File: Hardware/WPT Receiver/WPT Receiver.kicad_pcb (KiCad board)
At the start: 2 copper layers, 100 x 100 mm, 151 parts, among them J1 0.1" Header, J2 Tag-connect-NL, J3 0.1" Header, J4 0.1" Header, SW1 PTS647, SW2 PTS647, SW3 PTS647, U1 STM32G031C6U6, U10 74HC595, U2 INA180A3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

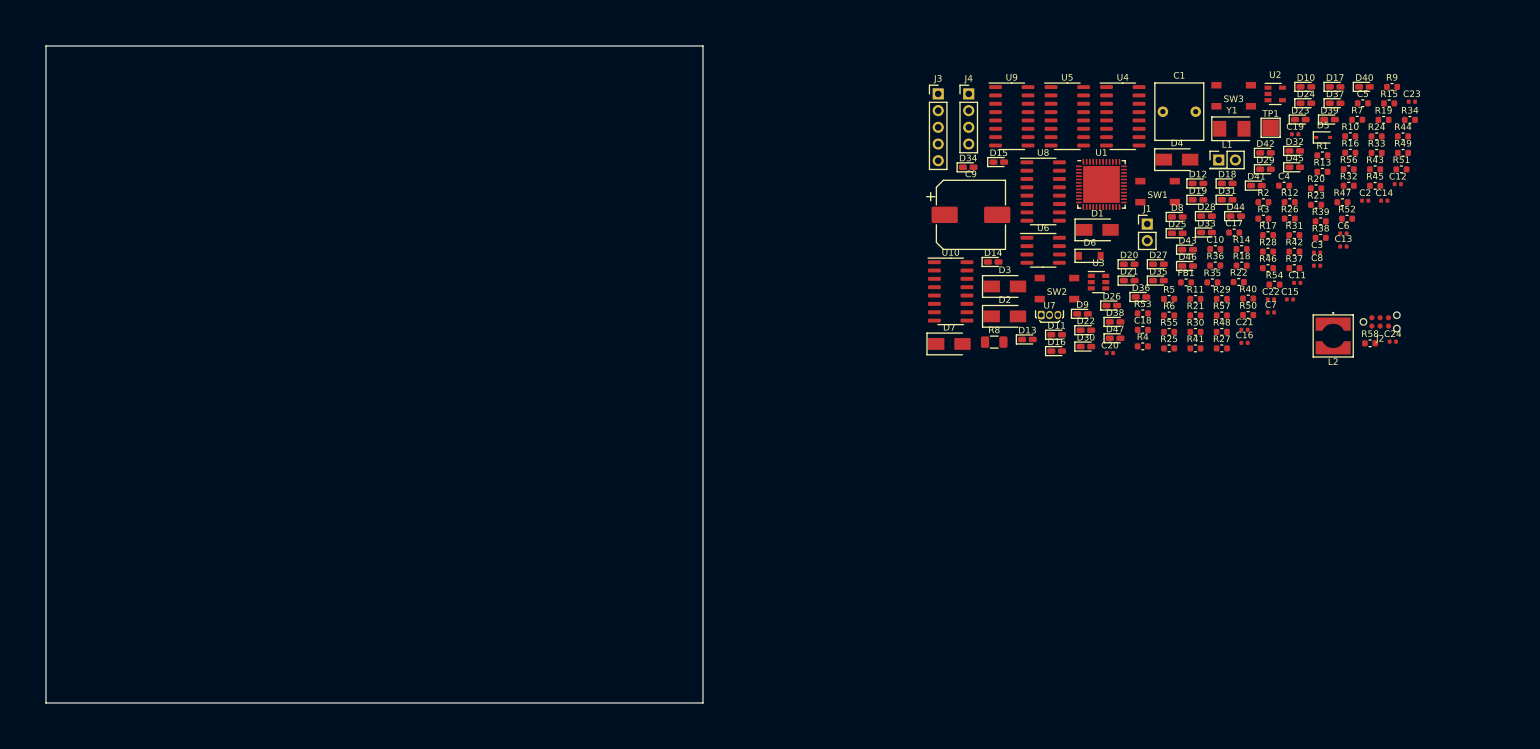
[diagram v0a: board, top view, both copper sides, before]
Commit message: started very rough part placement. Rounded board outline edges.
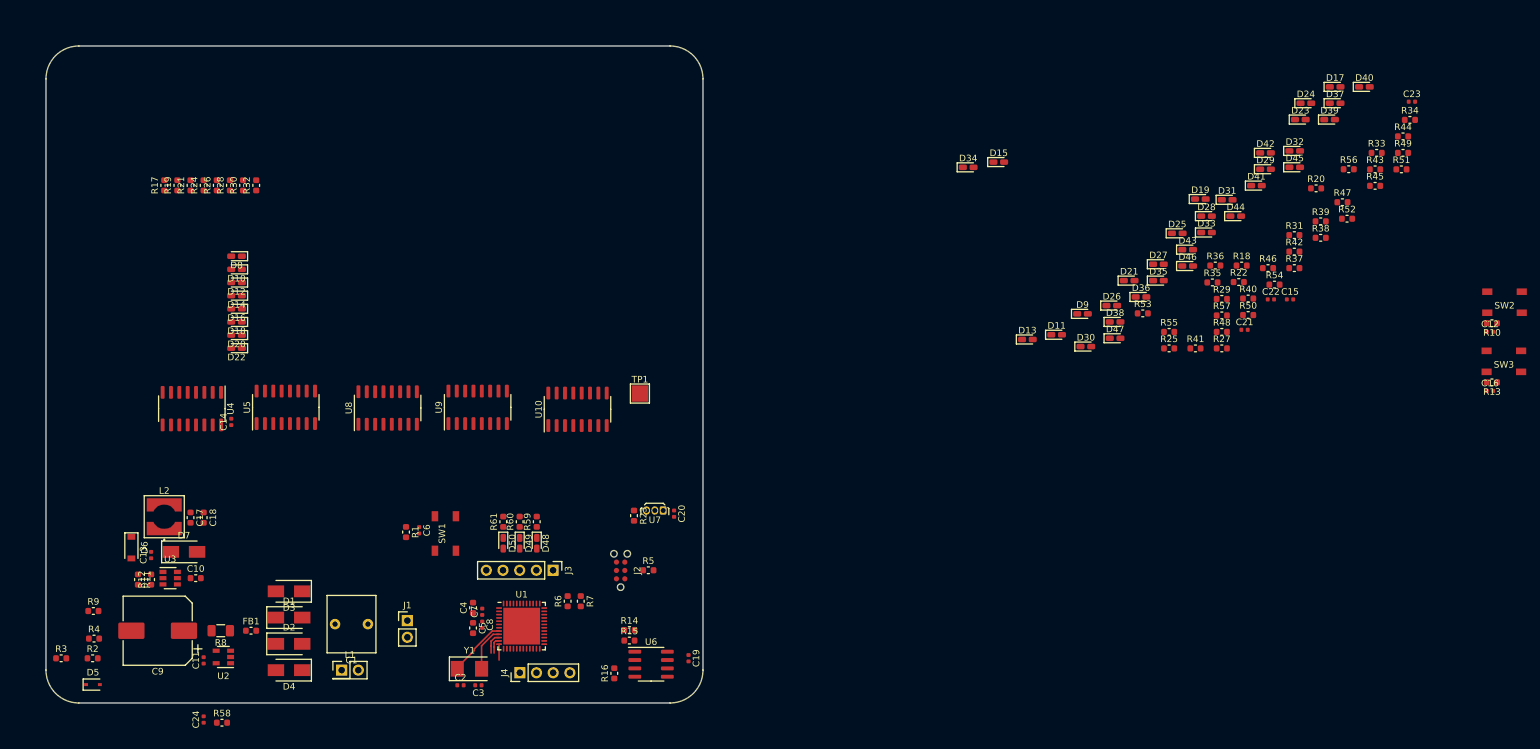
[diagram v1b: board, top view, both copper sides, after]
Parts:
- added D48: GRN, LED_SMD:LED_0603_1608Metric_Castellated, F.Cu at (124.7, 125.7)
- added D49: GRN, LED_SMD:LED_0603_1608Metric_Castellated, F.Cu at (122.1, 125.7)
- added D50: GRN, LED_SMD:LED_0603_1608Metric_Castellated, F.Cu at (119.6, 125.7)
- added R59: 680, Resistor_SMD:R_0603_1608Metric, F.Cu at (124.7, 122.4)
- added R60: 680, Resistor_SMD:R_0603_1608Metric, F.Cu at (122.1, 122.4)
- added R61: 680, Resistor_SMD:R_0603_1608Metric, F.Cu at (119.6, 122.4)
- moved R9 213.2 mm to (57.2, 136.0)
- moved D5 204.9 mm to (57.1, 147.2)
- moved R3 194.8 mm to (52.3, 143.2)
- moved R2 191.2 mm to (57.1, 143.2)
- moved C24 189.9 mm to (74.0, 152.5), turned to 90 degrees
- moved C13 187.5 mm to (66.0, 127.5), turned to 90 degrees
- moved R58 184.0 mm to (76.8, 153.0)
- moved R19 183.9 mm to (70.0, 71.2), turned to 90 degrees
- moved R12 182.6 mm to (66.0, 131.2), turned to 90 degrees
- moved U2 181.6 mm to (77.0, 143.0), turned to 180 degrees
- moved L2 180.0 mm to (68.0, 121.7), turned to 180 degrees
- moved C14 178.7 mm to (78.2, 107.2), turned to 90 degrees
- moved R24 178.7 mm to (74.0, 71.2), turned to 90 degrees
- moved C11 176.1 mm to (74.0, 143.5), turned to 90 degrees
- moved R17 168.2 mm to (68.0, 71.2), turned to 90 degrees
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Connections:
- net /GPIO1 renamed /LD1
- net /GPIO2 renamed /LD2
- net /GPIO3 renamed /LD3
- net Net-(D1-Pad1) renamed /VSYS_H
- net Net-(FB1-Pad1) renamed /VSYS_L
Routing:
- net Net-(C2-Pad1): track 0.00 -> 9.44 mm
- net Net-(C3-Pad1): track 0.00 -> 6.89 mm
- net /RST: track 0.00 -> 3.23 mm
- net /USER_BTN1: track 0.00 -> 2.47 mm
- net /ISENSE: track 0.00 -> 2.41 mm
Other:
- outline, holes or cut-outs redrawn

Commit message: Positioned non-power components, and routed most signals for peripherals other than shift regs/drivers. Added folder for 3D models for switch and crystal
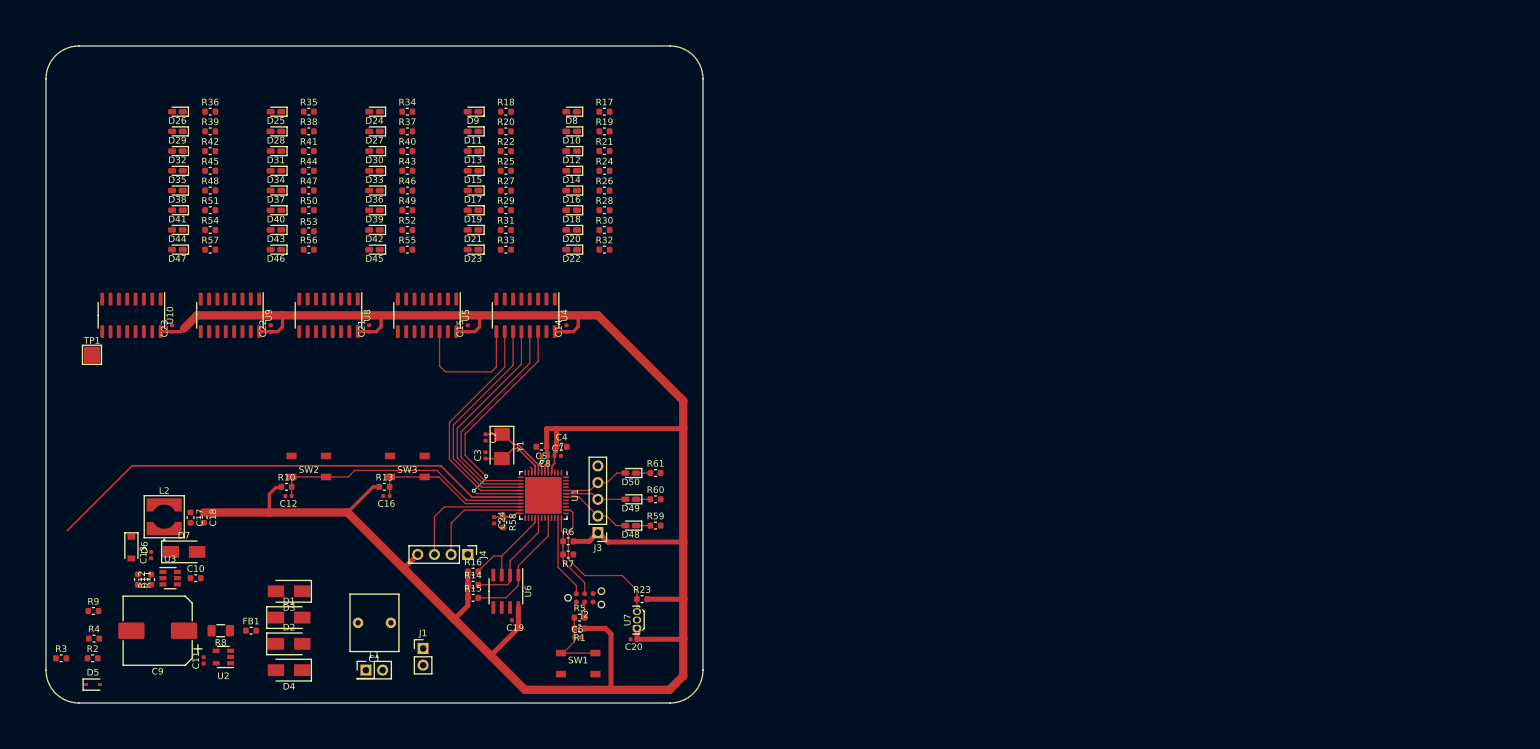
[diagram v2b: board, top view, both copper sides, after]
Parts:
- moved C23 191.8 mm to (69.2, 93.0), turned to 90 degrees
- moved R10 185.2 mm to (86.6, 117.1), turned to 0 degrees
- moved C12 184.6 mm to (86.9, 118.5), turned to 180 degrees
- moved SW2 183.7 mm to (90.0, 114.0)
- moved R51 181.4 mm to (75.0, 75.0)
- moved R45 177.3 mm to (75.0, 69.0)
- moved D32 170.1 mm to (70.0, 66.0), turned to 180 degrees
- moved R39 169.6 mm to (75.0, 63.0)
- moved R13 169.3 mm to (101.5, 117.1), turned to 0 degrees
- moved C16 168.7 mm to (101.8, 118.5), turned to 180 degrees
- moved SW3 167.7 mm to (105.0, 114.0)
- moved D40 166.7 mm to (85.0, 75.0), turned to 180 degrees
- moved R44 166.6 mm to (90.0, 69.0)
- moved D29 165.7 mm to (70.0, 63.0), turned to 180 degrees
- moved R42 165.7 mm to (75.0, 66.0)
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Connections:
- J4 pad 1: +3V3 -> GND
- J4 pad 2: /DEBUG_RX -> /DEBUG_TX
- J4 pad 3: /DEBUG_TX -> /DEBUG_RX
- J4 pad 4: GND -> +3V3
- U1 pad 11: /USER_BTN1 -> Net-(U1-Pad11)
- U1 pad 12: /ISENSE -> Net-(U1-Pad12)
- U1 pad 13: /VSENSE -> Net-(U1-Pad13)
- U1 pad 14: Net-(U1-Pad14) -> /SR_EN
- U1 pad 19: /SR_EN -> /VSENSE
- U1 pad 20: Net-(U1-Pad20) -> /USER_BTN1
- U1 pad 21: Net-(U1-Pad21) -> /USER_BTN2
- U1 pad 24: Net-(U1-Pad24) -> /ISENSE
- U1 pad 28: Net-(U1-Pad28) -> /TEMP_INT
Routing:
- net +3V3: track 0.00 -> 348.6 mm
- net /VSENSE: track 0.00 -> 75.1 mm
- net /SER_0: track 0.00 -> 38.3 mm, vias 0 -> 2
- net /USER_BTN1: track 2.47 -> 40.1 mm
- net /SRCLR: track 0.00 -> 35.7 mm
- net /SRCLK: track 0.00 -> 35.2 mm
- net /RCLK: track 0.00 -> 34.6 mm
- net /SR_EN: track 0.00 -> 34.0 mm
- net /USER_BTN2: track 0.00 -> 24.5 mm
- net /HALL_INT: track 0.00 -> 24.3 mm
- net /SER_0-1: track 0.00 -> 19.9 mm
- net /DEBUG_RX: track 0.00 -> 19.5 mm
- net /SDA: track 0.00 -> 19.0 mm
- net /SCL: track 0.00 -> 16.6 mm
- net /DEBUG_TX: track 0.00 -> 16.2 mm
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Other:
- rule trace_min: 0.2 -> 0.1

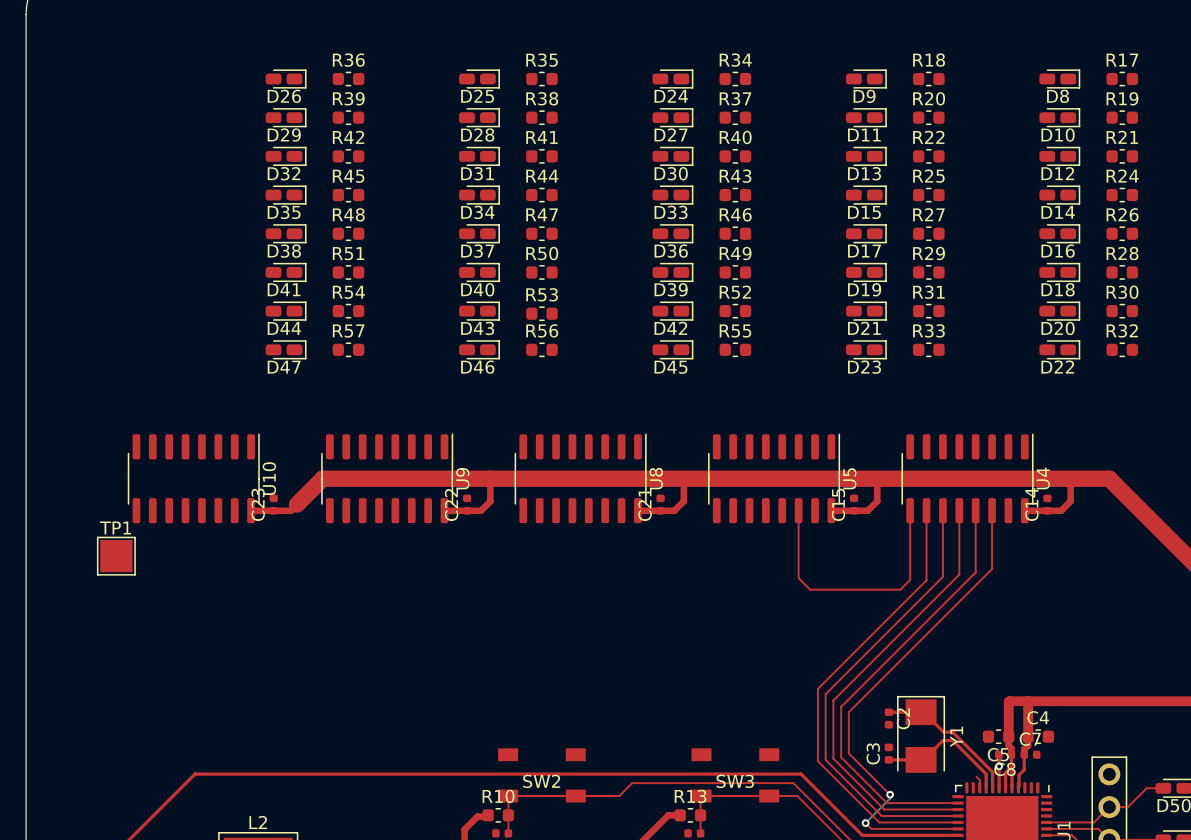
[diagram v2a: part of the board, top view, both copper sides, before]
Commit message: Routed all signals for shift regs and LEDs.
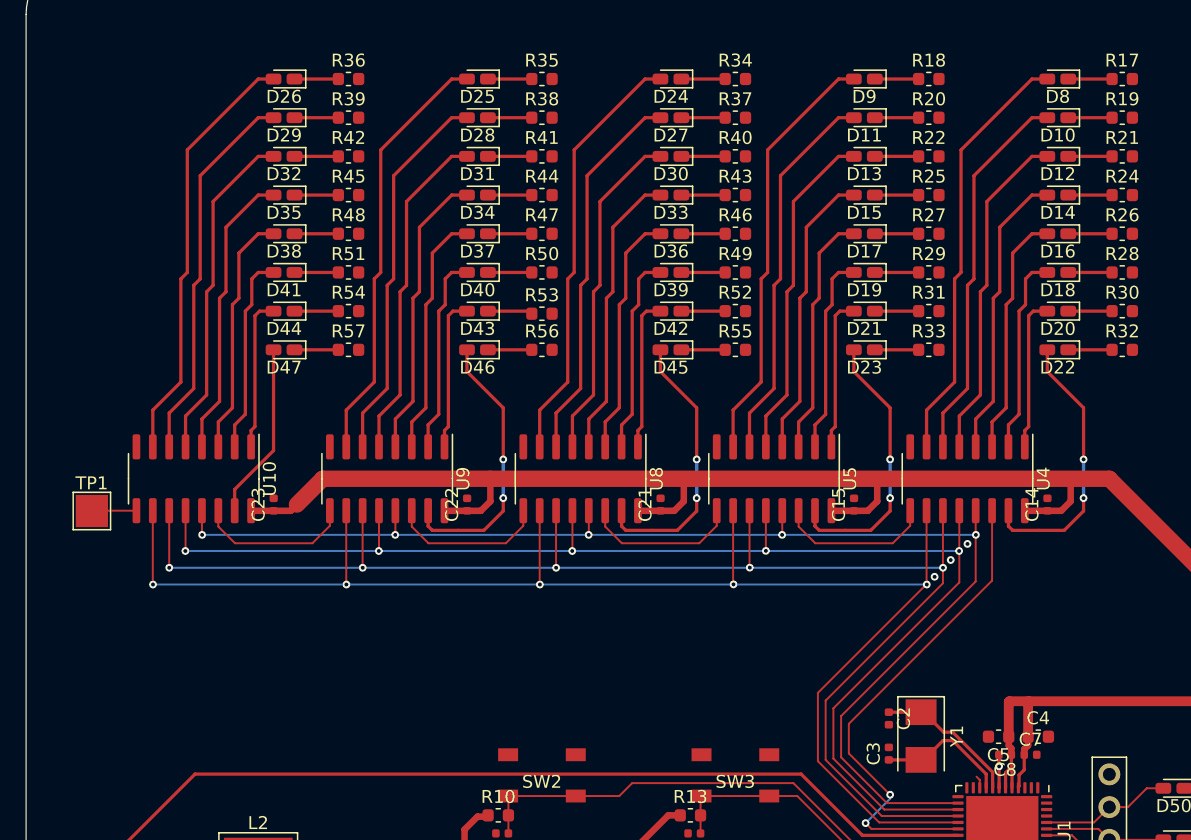
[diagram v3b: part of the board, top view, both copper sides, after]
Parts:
- moved TP1 3.98 mm to (55.1, 93.5)
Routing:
- net /SRCLR: track 35.7 -> 118.7 mm, vias 0 -> 5
- net /SRCLK: track 35.2 -> 112.9 mm, vias 0 -> 5
- net /RCLK: track 34.6 -> 107.2 mm, vias 0 -> 5
- net /SR_EN: track 34.0 -> 101.5 mm, vias 0 -> 5
- net Net-(D9-Pad2): track 0.00 -> 33.1 mm
- net Net-(D8-Pad2): track 0.00 -> 33.1 mm
- net Net-(D26-Pad2): track 0.00 -> 33.1 mm
- net Net-(D25-Pad2): track 0.00 -> 33.1 mm
- net Net-(D24-Pad2): track 0.00 -> 33.1 mm
- net Net-(D29-Pad2): track 0.00 -> 29.6 mm
- net Net-(D28-Pad2): track 0.00 -> 29.6 mm
- net Net-(D27-Pad2): track 0.00 -> 29.6 mm
- net Net-(D11-Pad2): track 0.00 -> 29.6 mm
- net Net-(D10-Pad2): track 0.00 -> 29.6 mm
- net Net-(D32-Pad2): track 0.00 -> 26.0 mm
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
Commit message: Added routing for power input region (including buck) and a few other remaining signals. All signals now routed other than ground
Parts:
- moved J1 13.9 mm to (94.1, 137.8)
- moved R9 11.5 mm to (68.2, 132.7)
- moved D5 10.6 mm to (55.5, 136.8)
- moved R2 4.93 mm to (55.2, 138.7)
- moved R3 3.11 mm to (55.2, 142.1), turned to 180 degrees
- moved R11 3.00 mm to (61.0, 131.1), turned to 0 degrees
- moved C11 2.96 mm to (76.0, 145.7), turned to 0 degrees
- moved R12 2.77 mm to (63.4, 130.2)
- moved R4 2.12 mm to (55.2, 140.3)
- moved C17 1.93 mm to (73.8, 122.6)
- moved D6 1.83 mm to (64.8, 126.0), turned to 90 degrees
- moved C18 1.58 mm to (75.3, 122.6)
- moved C10 1.35 mm to (71.8, 130.1)
- moved U3 1.35 mm to (67.9, 130.1)
- moved L2 1.25 mm to (69.2, 121.2)
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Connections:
- net Net-(C13-Pad2) renamed /BUCK_SW
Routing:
- net Net-(R58-Pad2): track 0.00 -> 145.8 mm, vias 0 -> 2
- net +3V3: track 348.6 -> 448.0 mm
- net VDC: track 0.00 -> 46.1 mm
- net /RST: track 12.7 -> 41.2 mm, vias 0 -> 2
- net /VSENSE: track 75.1 -> 92.9 mm
- net /IN-: track 0.00 -> 15.0 mm
- net /IN+: track 0.00 -> 11.9 mm
- net /VSYS_H: track 0.00 -> 9.46 mm
- net Net-(C1-Pad1): track 0.00 -> 7.72 mm
- net /VSYS_L: track 0.00 -> 6.71 mm
- net /BUCK_SW: track 0.00 -> 5.22 mm
- net Net-(R11-Pad2): track 0.00 -> 5.02 mm
- net Net-(C13-Pad1): track 0.00 -> 3.48 mm
- net Net-(R9-Pad2): track 0.00 -> 1.67 mm
- net /SRCLR: track 118.7 -> 117.9 mm, vias 5 -> 0
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- added copper zone on F.Cu, net +3V3
- added copper zone on F.Cu, net /BUCK_SW

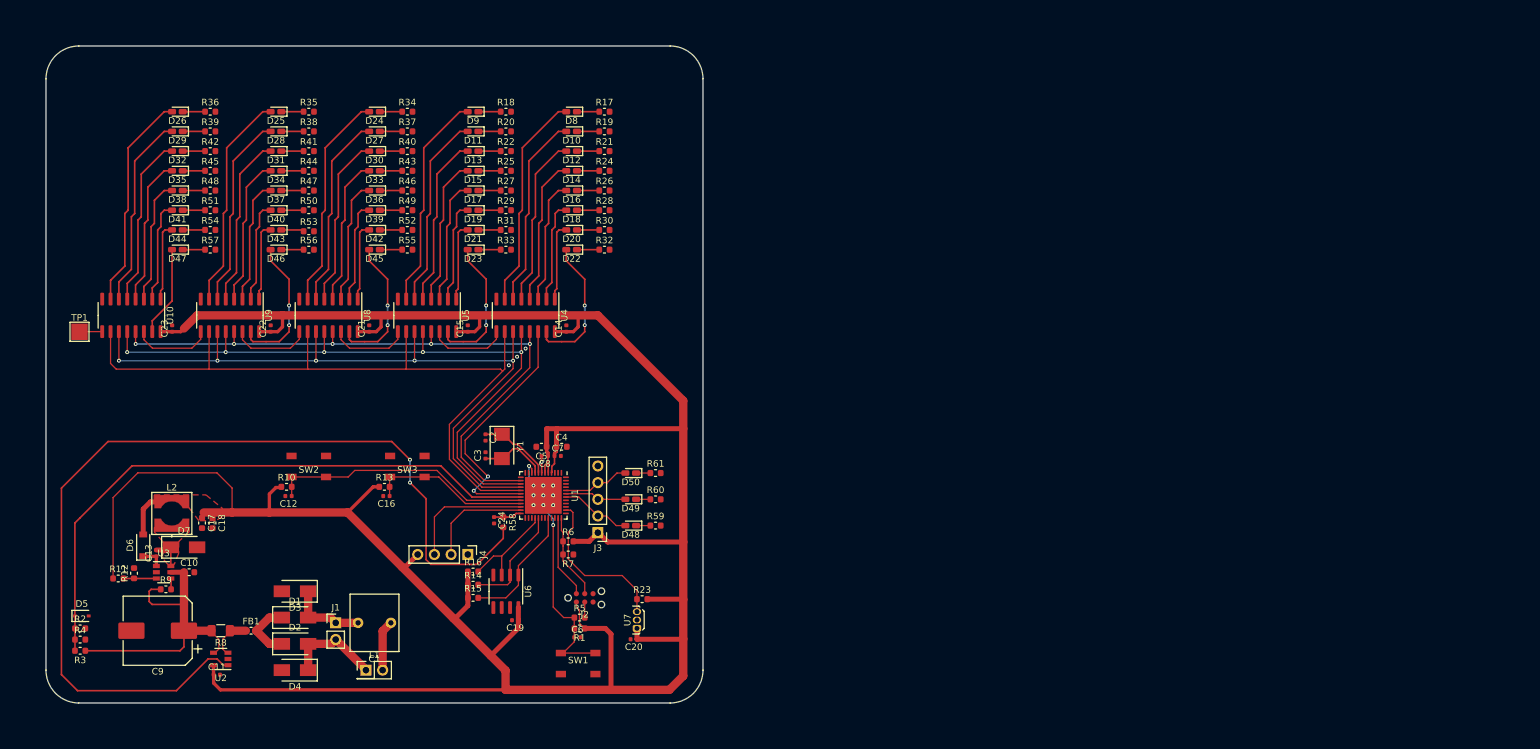
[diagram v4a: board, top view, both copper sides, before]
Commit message: added ground vias for all signals, and ground pour on bottom layer
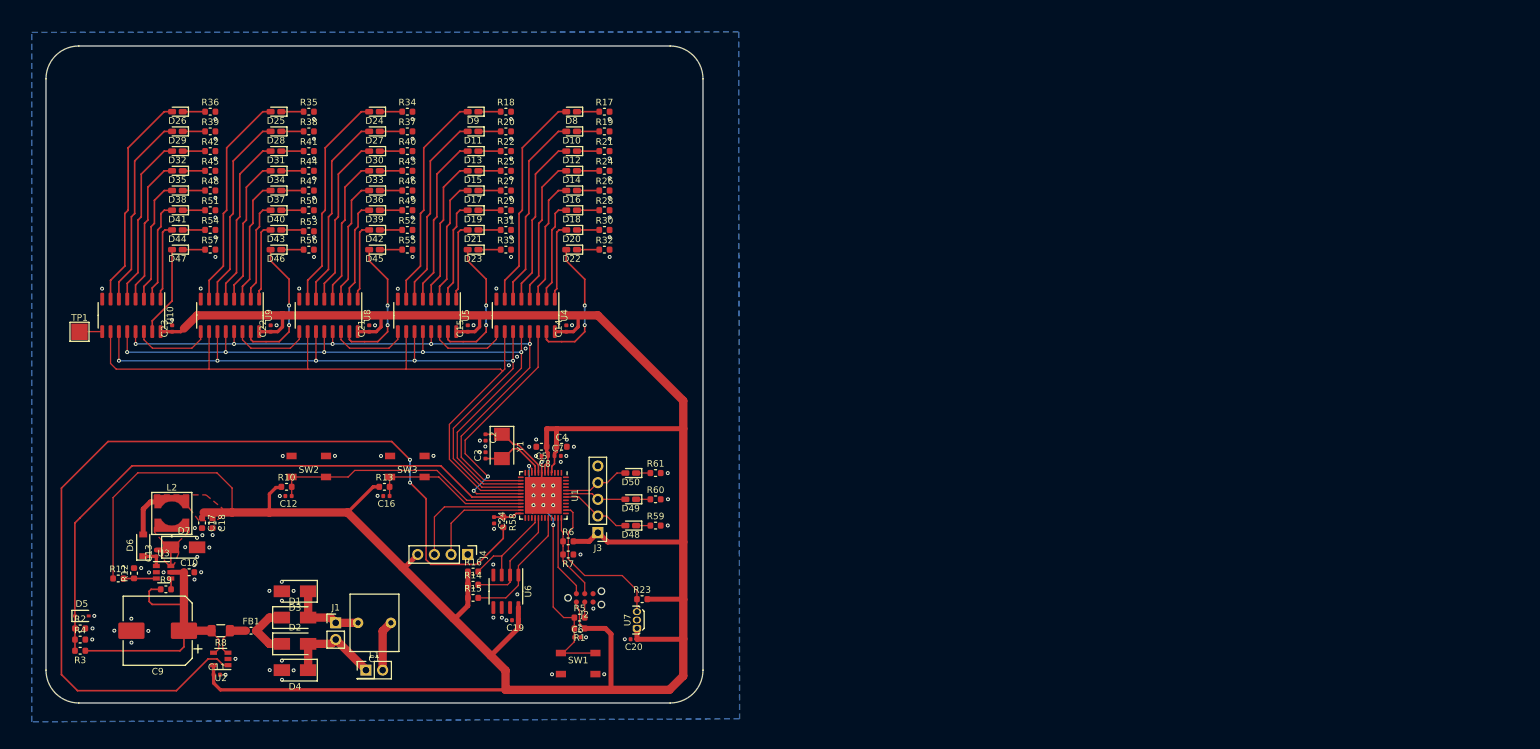
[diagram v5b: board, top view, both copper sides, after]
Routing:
- net GND: track 2.57 -> 6.11 mm, vias 13 -> 125
- added copper zone on B.Cu, net GND
